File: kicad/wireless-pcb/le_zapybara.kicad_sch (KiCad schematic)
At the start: 15 parts, among them J1 USB_C sink board 1.3mm, J3 TC2030_SWD, U3 PRTR5V0U2X, U7 nRF52840_E73-2G4M08S1C, Y1 Crystal_Small

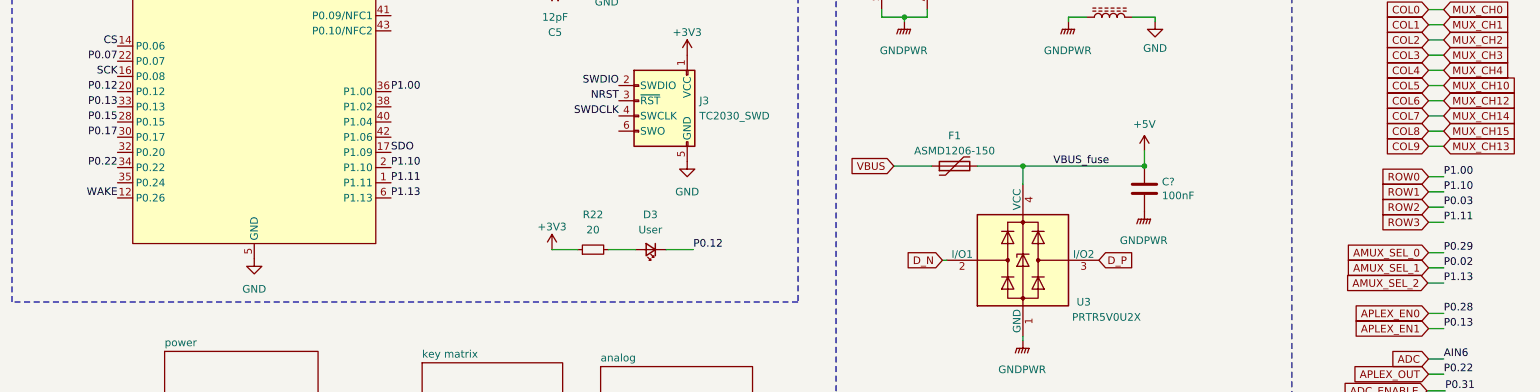
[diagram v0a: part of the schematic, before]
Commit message: Various cleanup, better pin selection, etc.
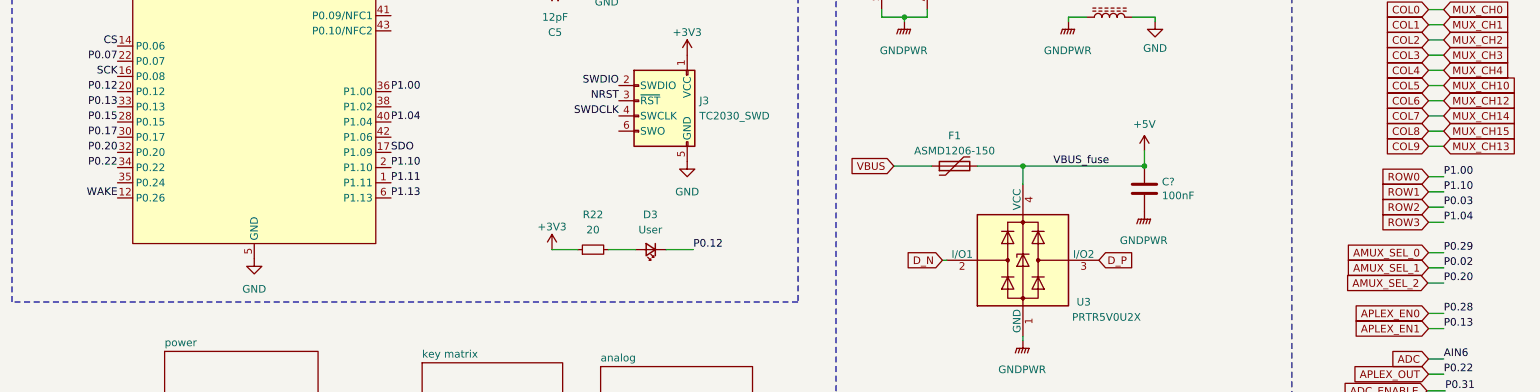
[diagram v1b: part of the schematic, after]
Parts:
- J3: now left out of the parts list
- Y1: LCSC (none) -> C97603
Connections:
- net AMUX_SEL_2: now also U7.32 (P0.20); no longer U7.6 (P1.13)
- net ROW3: now also U7.40 (P1.04); no longer U7.1 (P1.11)
- new net P1.11: U7.1 (P1.11)
- new net P1.13: U7.6 (P1.13)
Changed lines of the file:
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@@
     (effects (font (size 1.27 1.27)) (justify left bottom))
   )
-  (label "P1.13" (at 254 116.84 0) (fields_autoplaced)
+  (label "P0.20" (at 254 116.84 0) (fields_autoplaced)
     (effects (font (size 1.27 1.27)) (justify left bottom))
   )
@@
     (effects (font (size 1.27 1.27)) (justify left bottom))
   )
-  (label "P1.11" (at 254 106.68 0) (fields_autoplaced)
+  (label "P1.04" (at 254 106.68 0) (fields_autoplaced)
     (effects (font (size 1.27 1.27)) (justify left bottom))
   )
@@
     (effects (font (size 1.27 1.27)) (justify right bottom))
   )
+  (label "P1.04" (at 77.978 89.916 0) (fields_autoplaced)
+    (effects (font (size 1.27 1.27)) (justify left bottom))
+  )
   (label "NRST" (at 118.11 47.752 90) (fields_autoplaced)
     (effects (font (size 1.27 1.27)) (justify left bottom))
@@
   (label "P1.11" (at 77.978 100.076 0) (fields_autoplaced)
     (effects (font (size 1.27 1.27)) (justify left bottom))
+  )
+  (label "P0.20" (at 32.258 94.996 180) (fields_autoplaced)
+    (effects (font (size 1.27 1.27)) (justify right bottom))
   )
   (label "P0.15" (at 32.258 89.916 180) (fields_autoplaced)
@@
       (effects (font (size 1.27 1.27)) hide)
     )
+    (property "LCSC" "" (at 105.41 62.992 0)
+      (effects (font (size 1.27 1.27)) hide)
+    )
     (pin "2")
     (pin "1")
@@
   )
   (symbol (lib_id "PCM_marbastlib-various:TC2030_SWD") (at 122.428 88.9 0) (unit 1)
-    (in_bom yes) (on_board yes) (dnp no) (fields_autoplaced)
+    (in_bom no) (on_board yes) (dnp no) (fields_autoplaced)
     (property "Reference" "J3" (at 129.54 86.36 0)
       (effects (font (size 1.27 1.27)) (justify left))
@@
       (effects (font (size 1.27 1.27)) hide)
     )
+    (property "LCSC" "" (at 105.41 68.072 0)
+      (effects (font (size 1.27 1.27)) hide)
+    )
     (pin "2")
     (pin "1")
@@
       (effects (font (size 1.27 1.27)) hide)
     )
+    (property "LCSC" "C97603" (at 86.36 65.532 0)
+      (effects (font (size 1.27 1.27)) hide)
+    )

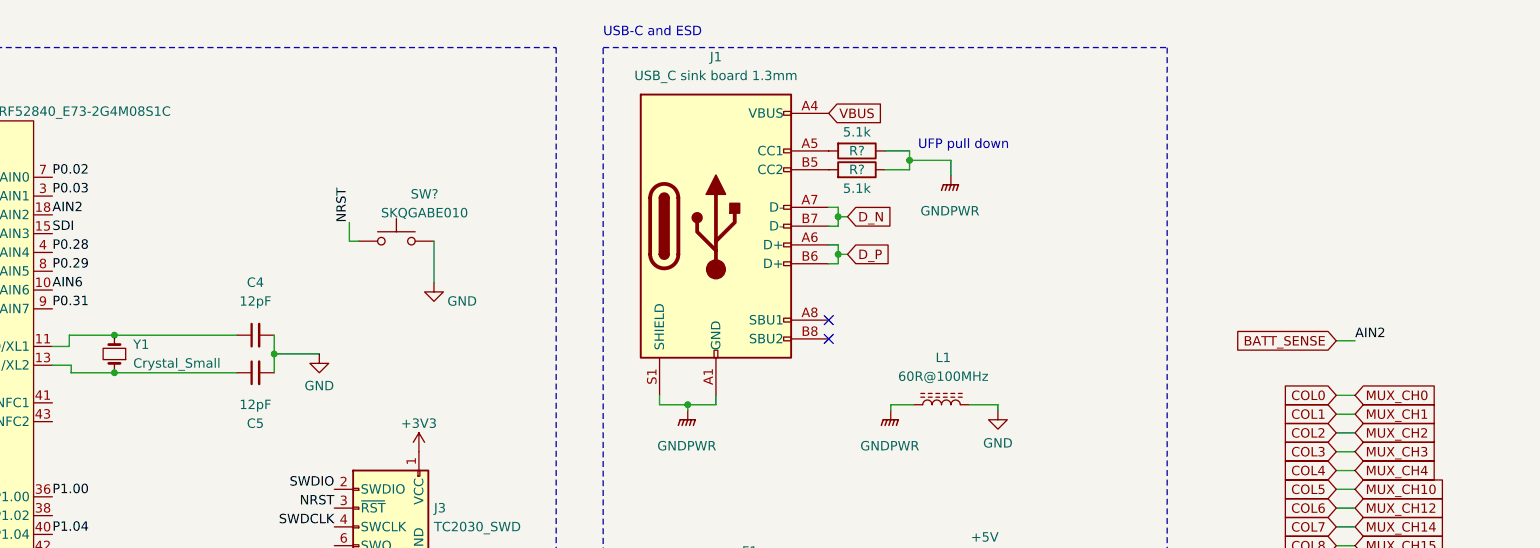
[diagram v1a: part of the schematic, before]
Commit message: BOM tweaks, add some test points, minor placement tweaks.
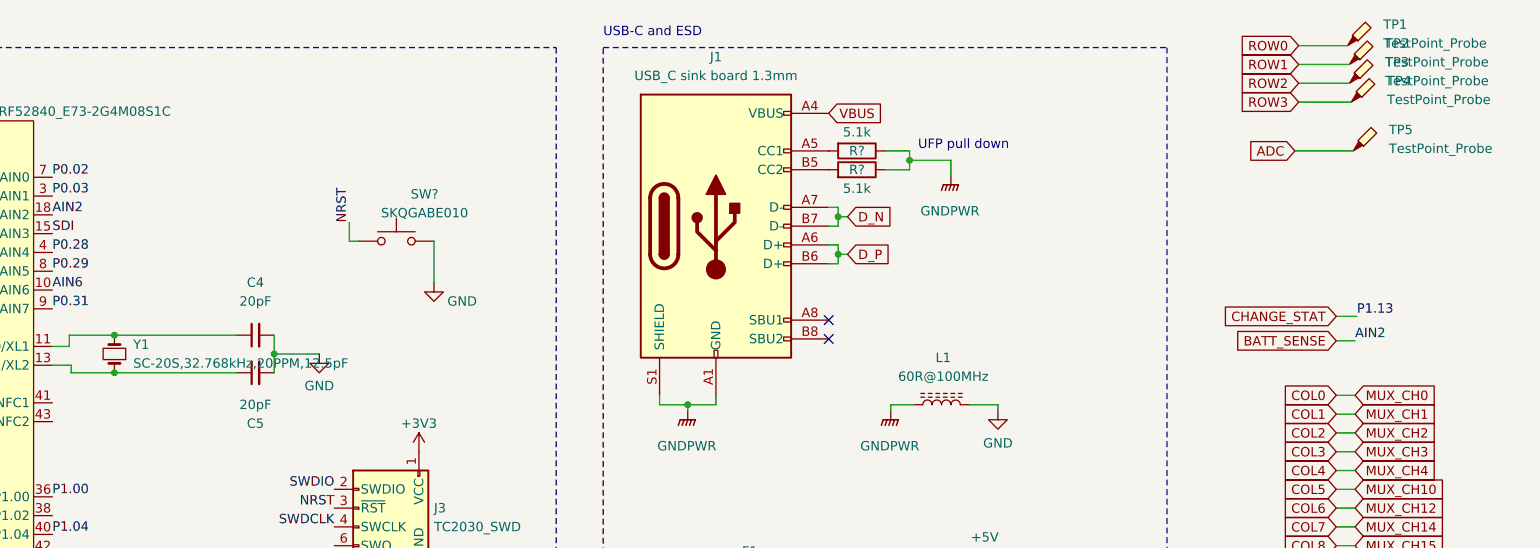
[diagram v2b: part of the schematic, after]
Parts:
- added TP1, TP2, TP3, TP4, TP5: TestPoint_Probe, TestPoint:TestPoint_Pad_D1.5mm, symbol Connector:TestPoint_Probe
- C4, C5: value 12pF -> 20pF
- Y1: value Crystal_Small -> SC-20S,32.768kHz,20PPM,12.5pF; footprint Crystal:Crystal_SMD_2012-2Pin_2.0x1.2mm_HandSoldering -> Crystal:Crystal_SMD_2012-2Pin_2.0x1.2mm; MPN (none) -> Seiko SC-20S
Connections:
- net ADC: now also TP5.1
- net ROW0: now also TP1.1
- net ROW1: now also TP2.1
- net ROW2: now also TP3.1
- net ROW3: now also TP4.1
- net P1.13 renamed CHANGE_STAT
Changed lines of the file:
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@@
+    (stroke (width 0) (type default))
+  )
+  (wire (pts (xy 251.46 60.452) (xy 254.254 60.452))
     (stroke (width 0) (type default))
   )
@@
     (stroke (width 0) (type default))
   )
+  (wire (pts (xy 246.38 28.956) (xy 253.238 28.956))
+    (stroke (width 0) (type default))
+  )
   (wire (pts (xy 163.83 72.39) (xy 167.64 72.39))
     (stroke (width 0) (type default))
@@
     (stroke (width 0) (type default))
   )
+  (wire (pts (xy 245.872 38.1) (xy 253.746 38.1))
+    (stroke (width 0) (type default))
+  )
   (wire (pts (xy 193.802 39.37) (xy 199.39 39.37))
     (stroke (width 0) (type default))
@@
     (stroke (width 0) (type default))
   )
+  (wire (pts (xy 246.38 23.876) (xy 252.984 23.876))
+    (stroke (width 0) (type default))
+  )
   (wire (pts (xy 190.5 40.64) (xy 193.802 40.64))
     (stroke (width 0) (type default))
@@
     (stroke (width 0) (type default))
   )
+  (wire (pts (xy 246.38 31.496) (xy 253.492 31.496))
+    (stroke (width 0) (type default))
+  )
   (wire (pts (xy 251.46 76.2) (xy 254 76.2))
     (stroke (width 0) (type default))
@@
   )
   (wire (pts (xy 251.206 144.526) (xy 254.254 144.526))
+    (stroke (width 0) (type default))
+  )
+  (wire (pts (xy 246.38 26.416) (xy 253.238 26.416))
     (stroke (width 0) (type default))
   )
@@
     (effects (font (size 1.27 1.27)) (justify left bottom))
   )
+  (label "P1.13" (at 254.254 60.452 0) (fields_autoplaced)
+    (effects (font (size 1.27 1.27)) (justify left bottom))
+  )
   (label "P1.13" (at 77.978 102.616 0) (fields_autoplaced)
     (effects (font (size 1.27 1.27)) (justify left bottom))
@@
     (effects (font (size 1.27 1.27)) (justify right))
     (property "Intersheetrefs" "${INTERSHEET_REFS}" (at 237.3085 116.7606 0)
+      (effects (font (size 1.27 1.27)) (justify right) hide)
+    )
+  )
+  (global_label "ROW1" (shape input) (at 246.38 26.416 180) (fields_autoplaced)
+    (effects (font (size 1.27 1.27)) (justify right))
+    (property "Intersheetrefs" "${INTERSHEET_REFS}" (at 238.2128 26.416 0)
       (effects (font (size 1.27 1.27)) (justify right) hide)
     )
@@
     )
   )
+  (global_label "ROW0" (shape input) (at 246.38 23.876 180) (fields_autoplaced)
+    (effects (font (size 1.27 1.27)) (justify right))
+    (property "Intersheetrefs" "${INTERSHEET_REFS}" (at 238.2128 23.876 0)
+      (effects (font (size 1.27 1.27)) (justify right) hide)
+    )
+  )
   (global_label "COL4" (shape input) (at 251.46 81.28 180) (fields_autoplaced)
     (effects (font (size 1.27 1.27)) (justify right))
     (property "Intersheetrefs" "${INTERSHEET_REFS}" (at 229.87 -50.8 0)
       (effects (font (size 1.27 1.27)) hide)
+    )
+  )
+  (global_label "ADC" (shape input) (at 245.872 38.1 180) (fields_autoplaced)
+    (effects (font (size 1.27 1.27)) (justify right))
+    (property "Intersheetrefs" "${INTERSHEET_REFS}" (at 239.3376 38.1 0)
+      (effects (font (size 1.27 1.27)) (justify right) hide)
     )
   )
@@
     )
   )
+  (global_label "CHANGE_STAT" (shape input) (at 251.46 60.452 180) (fields_autoplaced)
+    (effects (font (size 1.27 1.27)) (justify right))
+    (property "Intersheetrefs" "${INTERSHEET_REFS}" (at 235.8353 60.452 0)
+      (effects (font (size 1.27 1.27)) (justify right) hide)
+    )
+  )
   (global_label "MUX_CH13" (shape input) (at 254 93.98 0) (fields_autoplaced)
     (effects (font (size 1.27 1.27)) (justify left))
@@
     )
   )
+  (global_label "ROW2" (shape input) (at 246.38 28.956 180) (fields_autoplaced)
+    (effects (font (size 1.27 1.27)) (justify right))
+    (property "Intersheetrefs" "${INTERSHEET_REFS}" (at 238.2128 28.956 0)
+      (effects (font (size 1.27 1.27)) (justify right) hide)
+    )
+  )
   (global_label "APLEX_EN1" (shape input) (at 251.46 124.46 180) (fields_autoplaced)
     (effects (font (size 1.27 1.27)) (justify right))
     (property "Intersheetrefs" "${INTERSHEET_REFS}" (at 238.1524 124.46 0)
+      (effects (font (size 1.27 1.27)) (justify right) hide)
+    )
+  )
+  (global_label "ROW3" (shape input) (at 246.38 31.496 180) (fields_autoplaced)
+    (effects (font (size 1.27 1.27)) (justify right))
+    (property "Intersheetrefs" "${INTERSHEET_REFS}" (at 238.2128 31.496 0)
       (effects (font (size 1.27 1.27)) (justify right) hide)
     )
@@
         (path "/ca0d59d2-7f9b-4344-99bc-39bc2c8c88cb"
           (reference "D3") (unit 1)
+        )
+      )
+    )
+  )
+  (symbol (lib_id "Connector:TestPoint_Probe") (at 252.984 23.876 0) (unit 1)
+    (in_bom yes) (on_board yes) (dnp no) (fields_autoplaced)
+    (property "Reference" "TP1" (at 257.81 21.0185 0)
+      (effects (font (size 1.27 1.27)) (justify left))
+    )
+    (property "Value" "TestPoint_Probe" (at 257.81 23.5585 0)
+      (effects (font (size 1.27 1.27)) (justify left))
+    )
+    (property "Footprint" "TestPoint:TestPoint_Pad_D1.5mm" (at 258.064 23.876 0)
+      (effects (font (size 1.27 1.27)) hide)
+    )
+    (property "Datasheet" "~" (at 258.064 23.876 0)
+      (effects (font (size 1.27 1.27)) hide)
+    )
+    (pin "1")
+    (instances
+      (project "le_zapybara"
+        (path "/ca0d59d2-7f9b-4344-99bc-39bc2c8c88cb"
+          (reference "TP1") (unit 1)
         )
       )
@@
       (effects (font (size 1.27 1.27)))
     )
-    (property "Value" "12pF" (at 105.4163 58.42 90)
+    (property "Value" "20pF" (at 105.4163 58.42 90)
       (effects (font (size 1.27 1.27)))
     )
@@
     )
   )
+  (symbol (lib_id "Connector:TestPoint_Probe") (at 253.238 26.416 0) (unit 1)
+    (in_bom yes) (on_board yes) (dnp no) (fields_autoplaced)
+    (property "Reference" "TP2" (at 258.064 23.5585 0)
+      (effects (font (size 1.27 1.27)) (justify left))
+    )
+    (property "Value" "TestPoint_Probe" (at 258.064 26.0985 0)
+      (effects (font (size 1.27 1.27)) (justify left))
+    )
+    (property "Footprint" "TestPoint:TestPoint_Pad_D1.5mm" (at 258.318 26.416 0)
+      (effects (font (size 1.27 1.27)) hide)
+    )
+    (property "Datasheet" "~" (at 258.318 26.416 0)
+      (effects (font (size 1.27 1.27)) hide)
+    )
+    (pin "1")
+    (instances
+      (project "le_zapybara"
+        (path "/ca0d59d2-7f9b-4344-99bc-39bc2c8c88cb"
+          (reference "TP2") (unit 1)
+        )
+      )
+    )
+  )
   (symbol (lib_id "Device:R") (at 186.69 40.64 270) (mirror x) (unit 1)
     (in_bom yes) (on_board yes) (dnp no)
@@
     )
   )
+  (symbol (lib_id "Connector:TestPoint_Probe") (at 253.492 31.496 0) (unit 1)
+    (in_bom yes) (on_board yes) (dnp no) (fields_autoplaced)
+    (property "Reference" "TP4" (at 258.318 28.6385 0)
+      (effects (font (size 1.27 1.27)) (justify left))
+    )
+    (property "Value" "TestPoint_Probe" (at 258.318 31.1785 0)
+      (effects (font (size 1.27 1.27)) (justify left))
+    )
+    (property "Footprint" "TestPoint:TestPoint_Pad_D1.5mm" (at 258.572 31.496 0)
+      (effects (font (size 1.27 1.27)) hide)
+    )
+    (property "Datasheet" "~" (at 258.572 31.496 0)
+      (effects (font (size 1.27 1.27)) hide)
+    )
+    (pin "1")
+    (instances
+      (project "le_zapybara"
+        (path "/ca0d59d2-7f9b-4344-99bc-39bc2c8c88cb"
+          (reference "TP4") (unit 1)
+        )
+      )
+    )
+  )
+  (symbol (lib_id "Connector:TestPoint_Probe") (at 253.238 28.956 0) (unit 1)
+    (in_bom yes) (on_board yes) (dnp no) (fields_autoplaced)
+    (property "Reference" "TP3" (at 258.064 26.0985 0)
+      (effects (font (size 1.27 1.27)) (justify left))
+    )
+    (property "Value" "TestPoint_Probe" (at 258.064 28.6385 0)
+      (effects (font (size 1.27 1.27)) (justify left))
+    )
+    (property "Footprint" "TestPoint:TestPoint_Pad_D1.5mm" (at 258.318 28.956 0)
+      (effects (font (size 1.27 1.27)) hide)
+    )
+    (property "Datasheet" "~" (at 258.318 28.956 0)
+      (effects (font (size 1.27 1.27)) hide)
+    )
+    (pin "1")
+    (instances
+      (project "le_zapybara"
+        (path "/ca0d59d2-7f9b-4344-99bc-39bc2c8c88cb"
+          (reference "TP3") (unit 1)
+        )
+      )
+    )
+  )
   (symbol (lib_id "Device:C_Small") (at 105.41 68.072 90) (unit 1)
     (in_bom yes) (on_board yes) (dnp no)
@@
       (effects (font (size 1.27 1.27)))
     )
-    (property "Value" "12pF" (at 105.4164 72.39 90)
+    (property "Value" "20pF" (at 105.4164 72.39 90)
       (effects (font (size 1.27 1.27)))
     )
@@
       (effects (font (size 1.27 1.27)) (justify right))
     )
-    (property "Value" "Crystal_Small" (at 88.9 66.802 90)
+    (property "Value" "SC-20S,32.768kHz,20PPM,12.5pF" (at 88.9 66.802 90)
       (effects (font (size 1.27 1.27)) (justify right))
     )
-    (property "Footprint" "Crystal:Crystal_SMD_2012-2Pin_2.0x1.2mm_HandSoldering" (at 86.36 65.532 0)
+    (property "Footprint" "Crystal:Crystal_SMD_2012-2Pin_2.0x1.2mm" (at 86.36 65.532 0)
       (effects (font (size 1.27 1.27)) hide)
     )
@@
     )
     (property "LCSC" "C97603" (at 86.36 65.532 0)
+      (effects (font (size 1.27 1.27)) hide)
+    )
+    (property "MPN" "Seiko SC-20S" (at 86.36 65.532 90)
       (effects (font (size 1.27 1.27)) hide)
     )
@@
         )
       )
+    )
+  )
+  (symbol (lib_id "Connector:TestPoint_Probe") (at 253.746 38.1 0) (unit 1)
+    (in_bom yes) (on_board yes) (dnp no) (fields_autoplaced)
+    (property "Reference" "TP5" (at 258.572 35.2425 0)
+      (effects (font (size 1.27 1.27)) (justify left))
+    )
+    (property "Value" "TestPoint_Probe" (at 258.572 37.7825 0)
+      (effects (font (size 1.27 1.27)) (justify left))
+    )
+    (property "Footprint" "TestPoint:TestPoint_Pad_D1.5mm" (at 258.826 38.1 0)
+      (effects (font (size 1.27 1.27)) hide)
+    )
+    (property "Datasheet" "~" (at 258.826 38.1 0)
+      (effects (font (size 1.27 1.27)) hide)
+    )
+    (pin "1")
+    (instances
+      (project "le_zapybara"
+        (path "/ca0d59d2-7f9b-4344-99bc-39bc2c8c88cb"
+          (reference "TP5") (unit 1)
+        )
+      )
